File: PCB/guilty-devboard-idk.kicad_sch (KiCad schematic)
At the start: 54 parts, among them J1 USB_C_Receptacle_USB2.0_16P, Q1 SP2038CNQ, U1 nRF54LM20A-QGAA, U2 SGM40567-4.2XG/TR, U3 Xiao nRF52840 Connectors, U5 FH9261-G3JH, U6 BD83070GWL-E2, Y1 32MHz, Y2 32.768kHz

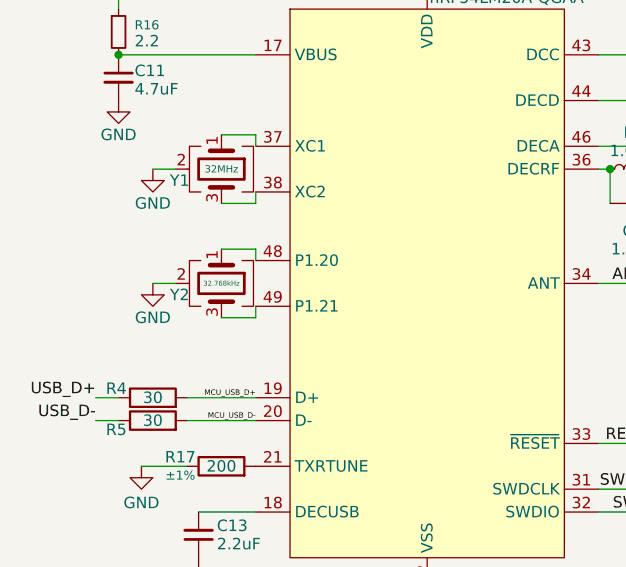
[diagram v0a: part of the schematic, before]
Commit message: use way smaller crystals and redo with space for bigger cap/inductor
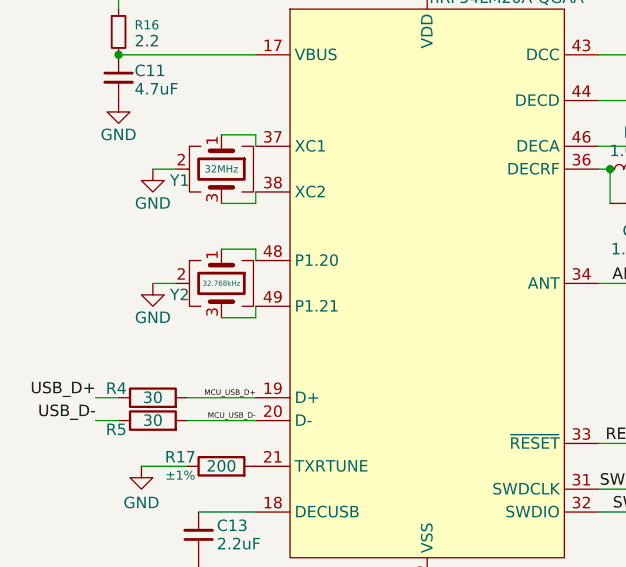
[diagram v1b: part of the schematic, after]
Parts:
- C1: footprint Capacitor_SMD:C_0201_0603Metric -> Capacitor_SMD:C_0402_1005Metric
- L3: footprint Inductor_SMD:L_0201_0603Metric -> Inductor_SMD:L_0603_1608Metric
- Y1, Y2: footprint Crystal:Crystal_SMD_2016-4Pin_2.0x1.6mm -> Crystal:Crystal_SMD_1210-4Pin_1.2x1.0mm
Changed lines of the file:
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@@
 			)
 		)
-		(property "Footprint" "Inductor_SMD:L_0201_0603Metric"
+		(property "Footprint" "Inductor_SMD:L_0603_1608Metric"
 			(at 251.46 45.72 0)
 			(hide yes)
@@
 			)
 		)
-		(property "Footprint" "Crystal:Crystal_SMD_2016-4Pin_2.0x1.6mm"
+		(property "Footprint" "Crystal:Crystal_SMD_1210-4Pin_1.2x1.0mm"
 			(at 34.29 52.07 0)
 			(hide yes)
@@
 			)
 		)
-		(property "Footprint" "Capacitor_SMD:C_0201_0603Metric"
+		(property "Footprint" "Capacitor_SMD:C_0402_1005Metric"
 			(at 48.26 25.4 0)
 			(hide yes)
@@
 			(effects
 				(font
-					(size 0.55 0.55)
+					(size 0.57 0.57)
 				)
 			)
 		)
-		(property "Footprint" "Crystal:Crystal_SMD_2016-4Pin_2.0x1.6mm"
+		(property "Footprint" "Crystal:Crystal_SMD_1210-4Pin_1.2x1.0mm"
 			(at 34.29 64.77 0)
 			(hide yes)

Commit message: tbh i have no idea what i cchanged but uh sure commit why not
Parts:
- removed Y1: 32MHz, Crystal:Crystal_SMD_1210-4Pin_1.2x1.0mm, symbol KiCad:Crystal_GND24
- removed Y2: 32.768kHz, Crystal:Crystal_SMD_1210-4Pin_1.2x1.0mm, symbol KiCad:Crystal_GND24
- added Y1: 32MHz, Crystal:Crystal_SMD_1210-4Pin_1.2x1.0mm, symbol KiCad:Crystal_GND2
- added Y2: 32.768kHz, Crystal:Crystal_SMD_1210-4Pin_1.2x1.0mm, symbol KiCad:Crystal_GND2
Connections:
- net GND: now also Y1.2, Y2.2
- net at U1.37 (XC1): now also Y1.1
- net at U1.38 (XC2): now also Y1.3
- net at U1.48 (P1.20): now also Y2.1
- net at U1.49 (P1.21): now also Y2.3
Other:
- moved on the sheet: R4, R5

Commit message: add tca9536 symbol and to schematic and whatever
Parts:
- added U4: (no value), symbol guilty-devboard:TCA9536
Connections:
- net +3V3: now also U4.7 (V_{CC})
- net GND: now also U4.3 (GND)
- net P1.30_A/D4_I2C_SDA: now also U4.6 (SDA)
- net P1.31_A/D5_I2C_SCL: now also U4.5 (SCL)

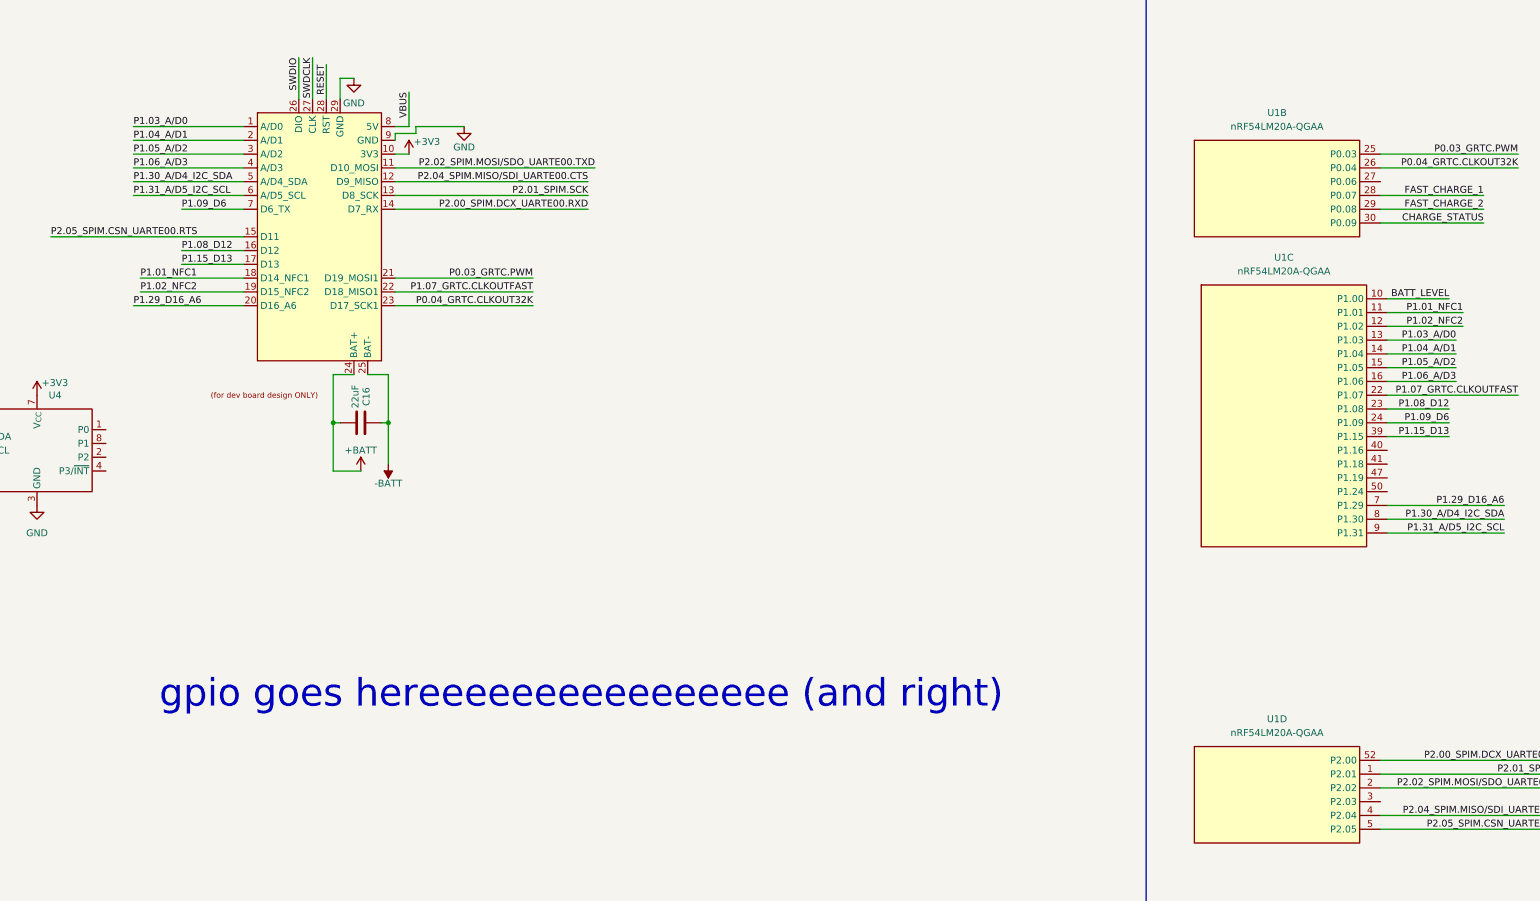
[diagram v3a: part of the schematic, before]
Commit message: add updated TCA9536 footprint (i dont know why it's updated tbh), and updated devboard symbol/footprint for xiao nrf54lm20a pads
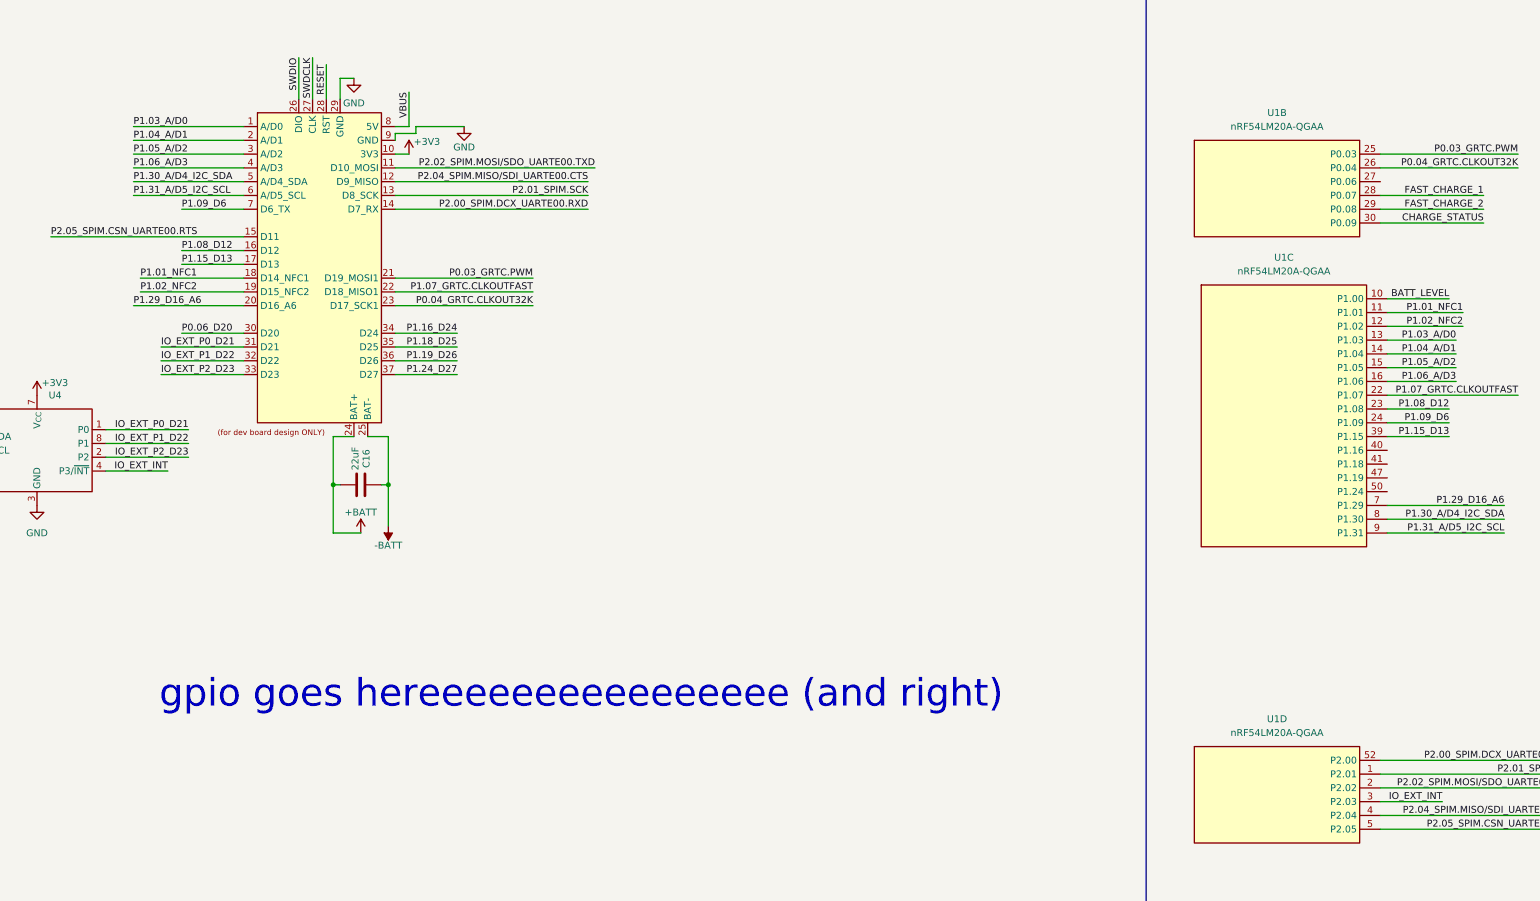
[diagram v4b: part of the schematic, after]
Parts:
- removed U3: Xiao nRF52840 Connectors, guilty-devboard-idk:Xiao nRF52840 Plus pads, symbol guilty-devboard:Xiao nRF52840 Plus Connectors (dev)
- added U3: Xiao nRF52840 Connectors, guilty-devboard-idk:Guilty Devboard Xrd pads, symbol guilty-devboard:Guilty Devboard Xrd Connectors (dev)
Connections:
- net +3V3: now also U3.10 (3V3)
- net +BATT: now also U3.24 (BAT+)
- net -BATT: now also U3.25 (BAT-)
- net GND: now also U3.29 (GND), U3.9 (GND)
- net P0.03_GRTC.PWM: now also U3.21 (D19_MOSI1)
- net P0.04_GRTC.CLKOUT32K: now also U3.23 (D17_SCK1)
- net P1.01_NFC1: now also U3.18 (D14_NFC1)
- net P1.02_NFC2: now also U3.19 (D15_NFC2)
- net P1.03_A/D0: now also U3.1 (A/D0)
- net P1.04_A/D1: now also U3.2 (A/D1)
- net P1.05_A/D2: now also U3.3 (A/D2)
- net P1.06_A/D3: now also U3.4 (A/D3)
- net P1.07_GRTC.CLKOUTFAST: now also U3.22 (D18_MISO1)
- net P1.08_D12: now also U3.16 (D12)
- net P1.09_D6: now also U3.7 (D6_TX)
- net P1.15_D13: now also U3.17 (D13)
- net P1.29_D16_A6: now also U3.20 (D16_A6)
- net P1.30_A/D4_I2C_SDA: now also U3.5 (A/D4_SDA)
- net P1.31_A/D5_I2C_SCL: now also U3.6 (A/D5_SCL)
- net P2.00_SPIM.DCX_UARTE00.RXD: now also U3.14 (D7_RX)
- net P2.01_SPIM.SCK: now also U3.13 (D8_SCK)
- net P2.02_SPIM.MOSI/SDO_UARTE00.TXD: now also U3.11 (D10_MOSI)
- net P2.04_SPIM.MISO/SDI_UARTE00.CTS: now also U3.12 (D9_MISO)
- net P2.05_SPIM.CSN_UARTE00.RTS: now also U3.15 (D11)
- net RESET: now also U3.28 (RST)
- net SWDCLK: now also U3.27 (CLK)
- net SWDIO: now also U3.26 (DIO)
- net VBUS: now also U3.8 (5V)
- net IO_EXT_INT: now reaches U1.3 (P2.03)
- net IO_EXT_INT: now also U4.4 (P3/~{INT})
- net IO_EXT_P0_D21: now reaches U4.1 (P0)
- net IO_EXT_P0_D21: now also U3.31 (D21)
- net IO_EXT_P2_D23: now reaches U4.2 (P2)
- net IO_EXT_P2_D23: now also U3.33 (D23)
- net IO_EXT_P1_D22: now reaches U4.8 (P1)
- net IO_EXT_P1_D22: now also U3.32 (D22)
- new net P0.06_D20: U3.30 (D20)
- new net P1.16_D24: U3.34 (D24)
- new net P1.18_D25: U3.35 (D25)
- new net P1.19_D26: U3.36 (D26)
- new net P1.24_D27: U3.37 (D27)
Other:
- moved on the sheet: C16

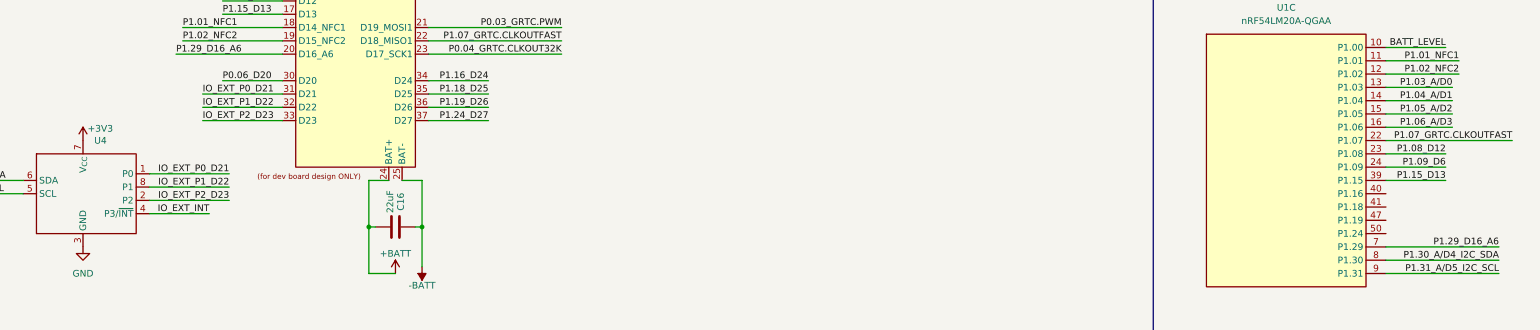
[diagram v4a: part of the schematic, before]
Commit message: route tca9536 and stuffffff
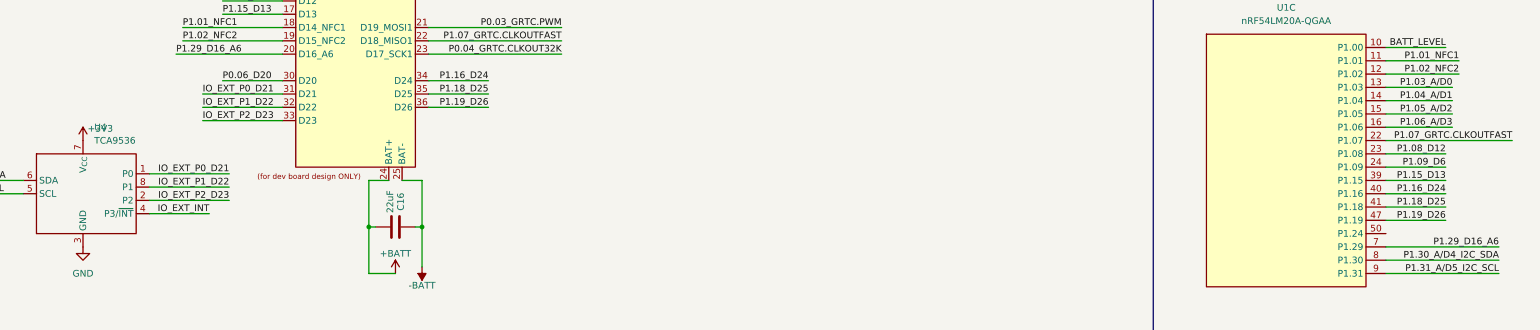
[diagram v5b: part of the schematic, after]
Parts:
- L6: footprint Inductor_SMD:L_0603_1608Metric -> Inductor_SMD:L_0402_1005Metric
- U4: value (none) -> TCA9536; footprint (none) -> guilty-devboard-idk:TCA9536
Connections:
- net P1.16_D24: now also U1.40 (P1.16)
- net P1.18_D25: now also U1.41 (P1.18)
- net P1.19_D26: now also U1.47 (P1.19)
- removed net P1.24_D27: U3.37 (D27)

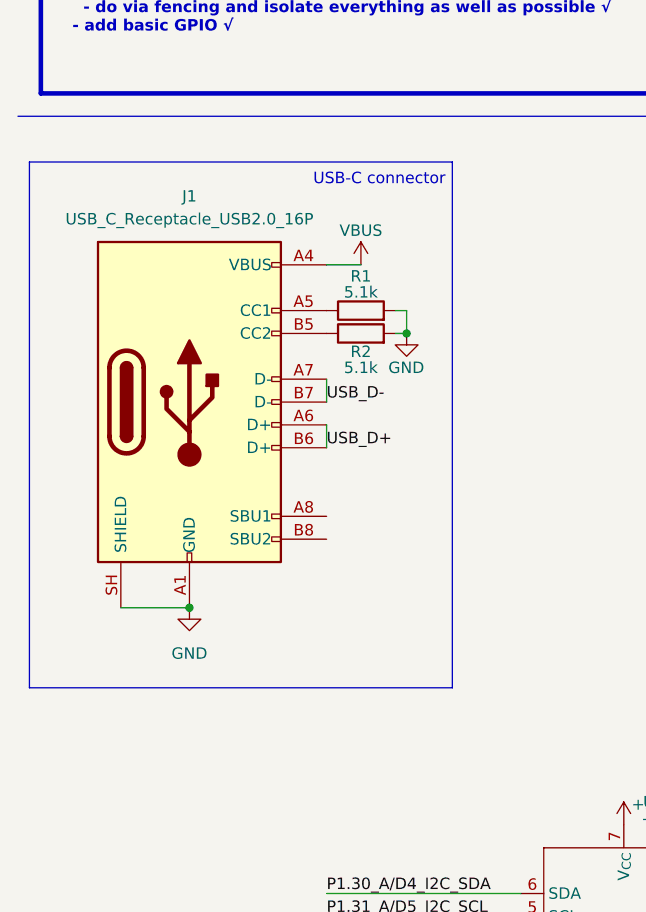
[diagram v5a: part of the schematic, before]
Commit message: add ferrite bead to shield usb-c
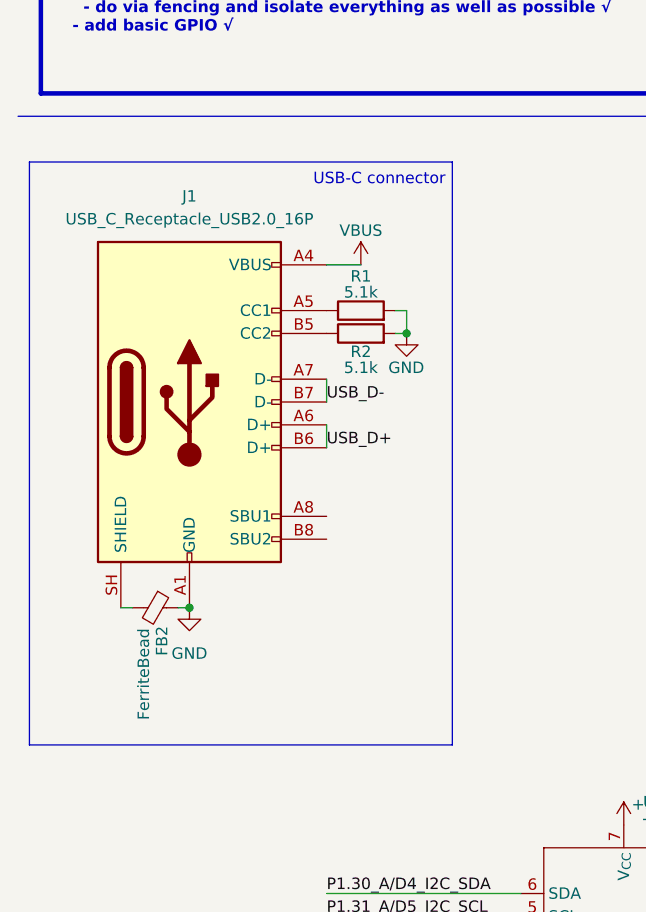
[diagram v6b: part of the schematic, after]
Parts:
- added FB2: FerriteBead, Inductor_SMD:L_0201_0603Metric, symbol KiCad:FerriteBead_Small
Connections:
- net GND: now also FB2.1; no longer J1.SH (SHIELD)
- new net: FB2.2, J1.SH (SHIELD)
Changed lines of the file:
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@@
 	(rectangle
 		(start 13.97 214.63)
-		(end 60.96 273.05)
+		(end 60.96 279.4)
 		(stroke
 			(width 0)
@@
 	(wire
 		(pts
+			(xy 30.48 264.16) (xy 31.75 264.16)
+		)
+		(stroke
+			(width 0)
+			(type default)
+		)
+	)
+	(wire
+		(pts
 			(xy 226.06 55.88) (xy 226.06 54.61)
 		)
@@
 	(wire
 		(pts
-			(xy 24.13 264.16) (xy 31.75 264.16)
+			(xy 24.13 264.16) (xy 25.4 264.16)
 		)
 		(stroke
@@
 					(unit 1)
 				)
+			)
+		)
+	)
+	(symbol
+		(lib_id "KiCad:FerriteBead_Small")
+		(at 27.94 264.16 270)
+		(unit 1)
+		(body_style 1)
+		(exclude_from_sim no)
+		(in_bom yes)
+		(on_board yes)
+		(in_pos_files yes)
+		(dnp no)
+		(property "Reference" "FB2"
+			(at 28.702 266.192 0)
+			(show_name no)
+			(do_not_autoplace no)
+			(effects
+				(font
+					(size 1.27 1.27)
+				)
+				(justify left)
+			)
+		)
+		(property "Value" "FerriteBead"
+			(at 26.67 266.446 0)
+			(show_name no)
+			(do_not_autoplace no)
+			(effects
+				(font
+					(size 1.27 1.27)
+				)
+				(justify left)
+			)
+		)
+		(property "Footprint" "Inductor_SMD:L_0201_0603Metric"
+			(at 27.94 262.382 90)
+			(hide yes)
+			(show_name no)
+			(do_not_autoplace no)
+			(effects
+				(font
+					(size 1.27 1.27)
+				)
+			)
+		)
+		(property "Datasheet" ""
+			(at 27.94 264.16 0)
+			(hide yes)
+			(show_name no)
+			(do_not_autoplace no)
+			(effects
+				(font
+					(size 1.27 1.27)
+				)
+			)
+		)
+		(property "Description" "Ferrite bead, small symbol"
+			(at 27.94 264.16 0)
+			(hide yes)
+			(show_name no)
+			(do_not_autoplace no)
+			(effects
+				(font
+					(size 1.27 1.27)
+				)
+			)
+		)
+		(pin "1"
+		)
+		(pin "2"
+		)
+		(instances
+			(project "guilty-devboard-idk"
+				(path "/f655de09-440b-4c8a-8451-7845142cd85d"
+					(reference "FB2")
+					(unit 1)
+				)
